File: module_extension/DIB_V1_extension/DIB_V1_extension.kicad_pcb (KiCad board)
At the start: 2 copper layers, 76.1 x 51.5 mm, 12 parts, among them J1 20-pin power socket, J2 28-pin module socket, J3 PROBE, J4 CABLE, J5 PROBE, J6 CABLE

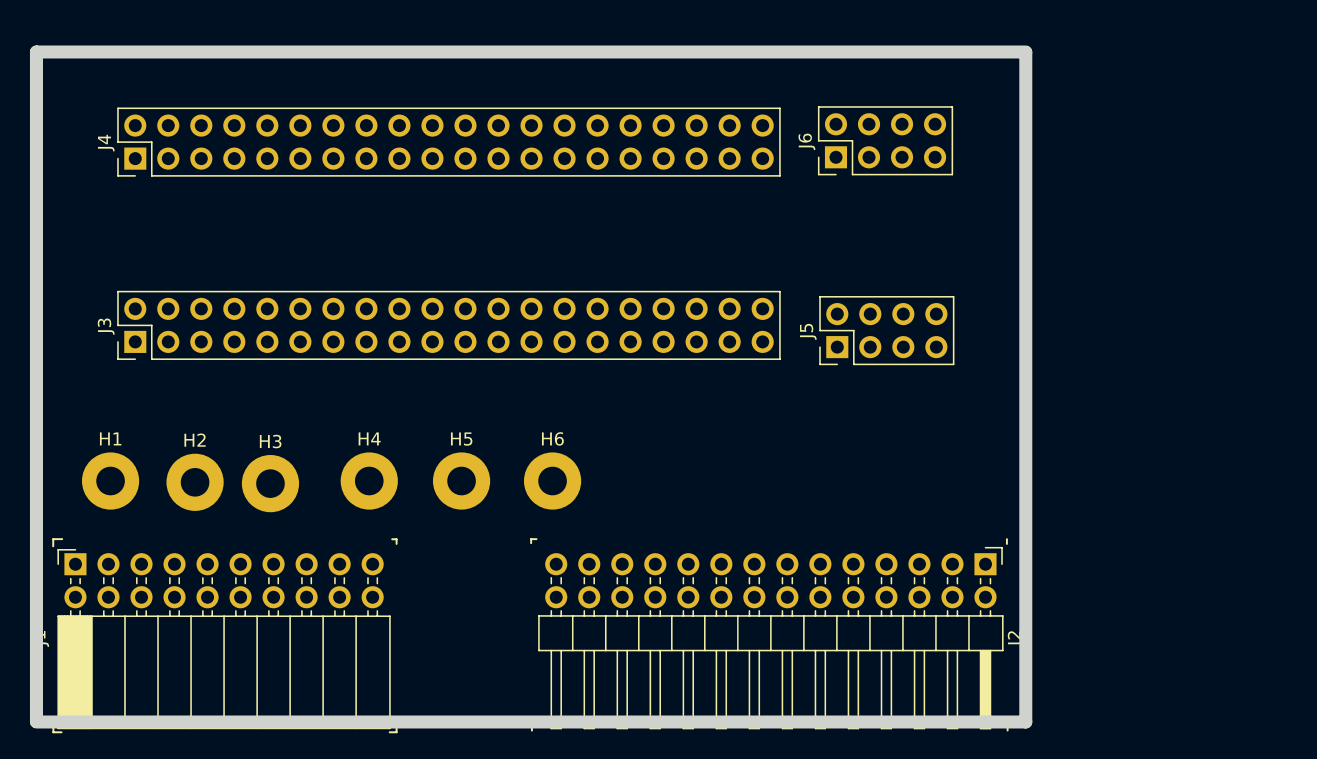
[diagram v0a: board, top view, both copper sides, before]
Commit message: Finished routing, adding pictures and README
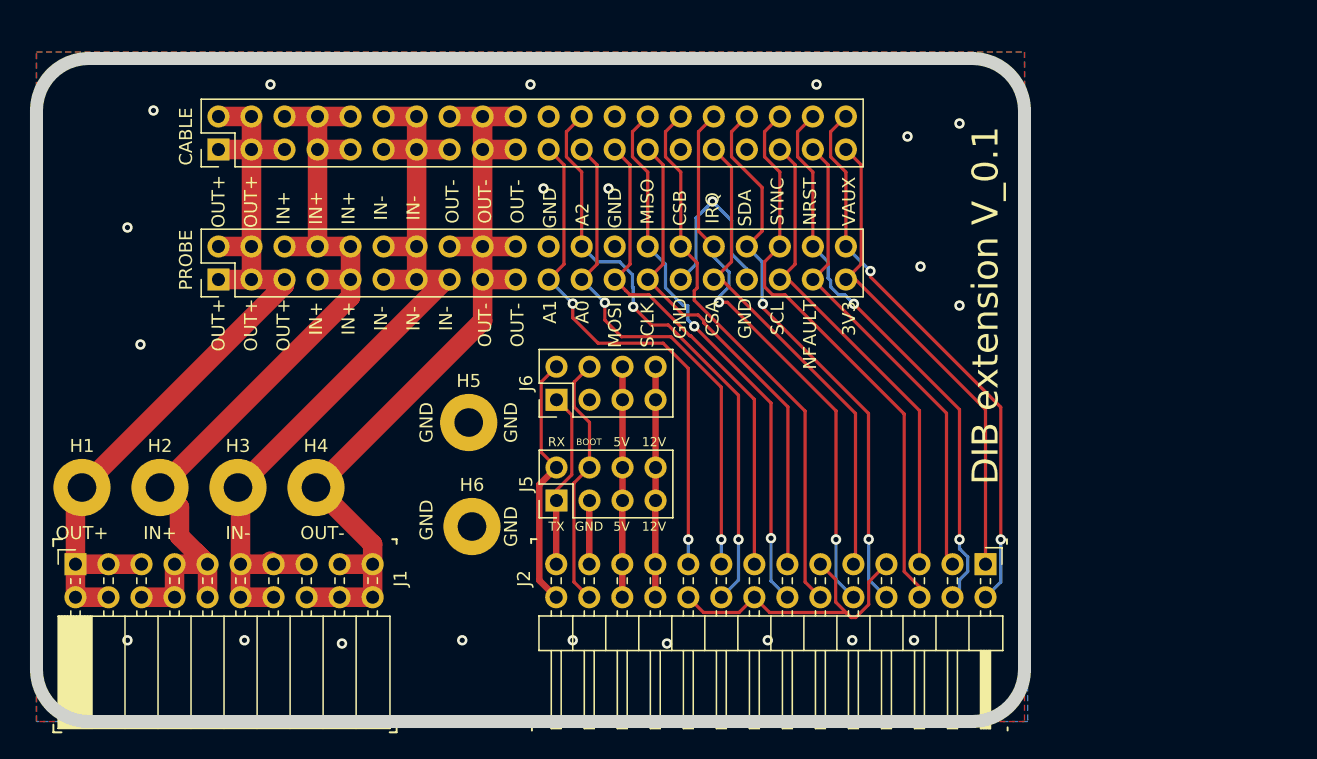
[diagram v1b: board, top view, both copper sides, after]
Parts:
- moved J6 28.5 mm to (113.3, 110.8)
- moved J5 24.6 mm to (113.3, 118.6)
- moved J3 8.00 mm to (87.3, 101.6)
- moved H6 7.12 mm to (106.8, 120.6)
- moved J4 6.44 mm to (87.3, 91.6)
- moved H5 4.53 mm to (106.5, 112.6)
- moved H4 4.13 mm to (94.8, 117.6)
- moved H2 2.73 mm to (82.8, 117.6)
- moved H3 2.52 mm to (88.8, 117.6)
- moved H1 2.26 mm to (76.8, 117.6)
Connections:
- J2 pad 1: (no net) -> DIB_+3V3
- J2 pad 10: (no net) -> DIB_IRQ
- J2 pad 12: (no net) -> DIB_CSB
- J2 pad 13: (no net) -> DIB_SCLK
- J2 pad 14: (no net) -> DIB_MISO
- J2 pad 15: (no net) -> DIB_MOSI
- J2 pad 17: (no net) -> DIB_A0
- J2 pad 18: (no net) -> DIB_A2
- J2 pad 19: (no net) -> DIB_A1
- J2 pad 2: (no net) -> +VAUX
- J2 pad 26: (no net) -> DIB_BOOT
- J2 pad 27: (no net) -> UART_TX
- J2 pad 28: (no net) -> UART_RX
- J2 pad 3: (no net) -> DIB_NFAULT
- J2 pad 4: (no net) -> DIB_NRESET
- J2 pad 5: (no net) -> DIB_SCL
- J2 pad 6: (no net) -> DIB_SYNC
- J2 pad 8: (no net) -> DIB_SDA
- J2 pad 9: (no net) -> DIB_CSA
- J3 pad 1: (no net) -> OUT+
- J3 pad 10: (no net) -> IN+
- J3 pad 11: (no net) -> IN-
- J3 pad 12: (no net) -> IN-
- J3 pad 13: (no net) -> IN-
- J3 pad 14: (no net) -> IN-
- J3 pad 15: (no net) -> IN-
- J3 pad 16: (no net) -> OUT-
- J3 pad 17: (no net) -> OUT-
- J3 pad 18: (no net) -> OUT-
- J3 pad 19: (no net) -> OUT-
- J3 pad 2: (no net) -> OUT+
- J3 pad 20: (no net) -> OUT-
- J3 pad 21: (no net) -> DIB_A1
- J3 pad 22: (no net) -> GND
- J3 pad 23: (no net) -> DIB_A0
- J3 pad 24: (no net) -> DIB_A2
- J3 pad 25: (no net) -> DIB_MOSI
- J3 pad 26: (no net) -> GND
- J3 pad 27: (no net) -> DIB_SCLK
- J3 pad 28: (no net) -> DIB_MISO
- J3 pad 29: (no net) -> GND
- J3 pad 3: (no net) -> OUT+
- J3 pad 30: (no net) -> DIB_CSB
- J3 pad 31: (no net) -> DIB_CSA
- J3 pad 32: (no net) -> DIB_IRQ
- J3 pad 33: (no net) -> GND
- J3 pad 34: (no net) -> DIB_SDA
- J3 pad 35: (no net) -> DIB_SCL
- J3 pad 36: (no net) -> DIB_SYNC
- J3 pad 37: (no net) -> DIB_NFAULT
- J3 pad 38: (no net) -> DIB_NRESET
- J3 pad 39: (no net) -> DIB_+3V3
- J3 pad 4: (no net) -> OUT+
- J3 pad 40: (no net) -> +VAUX
- J3 pad 5: (no net) -> OUT+
- J3 pad 6: (no net) -> IN+
- J3 pad 7: (no net) -> IN+
- J3 pad 8: (no net) -> IN+
- J3 pad 9: (no net) -> IN+
- J4 pad 1: (no net) -> OUT+
- J4 pad 10: (no net) -> IN+
- J4 pad 11: (no net) -> IN-
- J4 pad 12: (no net) -> IN-
- J4 pad 13: (no net) -> IN-
- J4 pad 14: (no net) -> IN-
- J4 pad 15: (no net) -> IN-
- J4 pad 16: (no net) -> OUT-
- J4 pad 17: (no net) -> OUT-
- J4 pad 18: (no net) -> OUT-
- J4 pad 19: (no net) -> OUT-
- J4 pad 2: (no net) -> OUT+
- J4 pad 20: (no net) -> OUT-
- J4 pad 21: (no net) -> DIB_A1
- J4 pad 22: (no net) -> GND
- J4 pad 23: (no net) -> DIB_A0
- J4 pad 24: (no net) -> DIB_A2
- J4 pad 25: (no net) -> DIB_MOSI
- J4 pad 26: (no net) -> GND
- J4 pad 27: (no net) -> DIB_SCLK
- J4 pad 28: (no net) -> DIB_MISO
- J4 pad 29: (no net) -> GND
- J4 pad 3: (no net) -> OUT+
- J4 pad 30: (no net) -> DIB_CSB
- J4 pad 31: (no net) -> DIB_CSA
- J4 pad 32: (no net) -> DIB_IRQ
- J4 pad 33: (no net) -> GND
- J4 pad 34: (no net) -> DIB_SDA
- J4 pad 35: (no net) -> DIB_SCL
- J4 pad 36: (no net) -> DIB_SYNC
- J4 pad 37: (no net) -> DIB_NFAULT
- J4 pad 38: (no net) -> DIB_NRESET
- J4 pad 39: (no net) -> DIB_+3V3
- J4 pad 4: (no net) -> OUT+
- J4 pad 40: (no net) -> +VAUX
- J4 pad 5: (no net) -> OUT+
- J4 pad 6: (no net) -> IN+
- J4 pad 7: (no net) -> IN+
- J4 pad 8: (no net) -> IN+
- J4 pad 9: (no net) -> IN+
- J5 pad 1: (no net) -> UART_TX
- J5 pad 2: (no net) -> UART_RX
- J5 pad 3: (no net) -> GND
- J5 pad 4: (no net) -> DIB_BOOT
- J5 pad 5: (no net) -> 5V
- J5 pad 6: (no net) -> 5V
- J5 pad 7: (no net) -> +12V
- J5 pad 8: (no net) -> +12V
- J6 pad 1: (no net) -> UART_TX
- J6 pad 2: (no net) -> UART_RX
- J6 pad 3: (no net) -> GND
- J6 pad 4: (no net) -> DIB_BOOT
- J6 pad 5: (no net) -> 5V
- J6 pad 6: (no net) -> 5V
- J6 pad 7: (no net) -> +12V
- J6 pad 8: (no net) -> +12V
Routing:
- net IN+: track 0.00 -> 68.8 mm
- net IN-: track 0.00 -> 67.2 mm
- net OUT-: track 0.00 -> 67.0 mm
- net OUT+: track 0.00 -> 66.5 mm
- net DIB_A2: track 0.00 -> 45.3 mm, vias 0 -> 2
- net DIB_SYNC: track 0.00 -> 43.9 mm
- net DIB_NRESET: track 0.00 -> 43.7 mm, vias 0 -> 2
- net DIB_IRQ: track 0.00 -> 43.4 mm, vias 0 -> 2
- net DIB_SDA: track 0.00 -> 43.4 mm, vias 0 -> 2
- net +VAUX: track 0.00 -> 43.4 mm, vias 0 -> 2
- net GND: track 0.00 -> 43.2 mm, vias 0 -> 22
- net DIB_MISO: track 0.00 -> 42.6 mm, vias 0 -> 2
- net DIB_CSB: track 0.00 -> 42.6 mm
- net DIB_A1: track 0.00 -> 40.3 mm, vias 0 -> 2
- net DIB_A0: track 0.00 -> 39.5 mm, vias 0 -> 2
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- added copper zone on B.Cu, net GND
- added copper zone on F.Cu, net GND
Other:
- board size 76.1 x 51.5 mm -> 76 x 51 mm
- board text added: "12V"
- board text added: "3V3"
- board text added: "5V"
- board text added: "A0"
- board text added: "A1"
- board text added: "A2"
- board text added: "BOOT"
- board text added: "CABLE"
- board text added: "CSA"
- board text added: "CSB"
- board text added: "DIB extension V_0.1"
- board text added: "GND"
- board text added: "IN+"
- board text added: "IN-"
- board text added: "IRQ"
- board text added: "MISO"
- board text added: "MOSI"
- board text added: "NFAULT"
- board text added: "NRST"
- board text added: "OUT+"
- board text added: "OUT-"
- board text added: "PROBE"
- board text added: "RX"
- board text added: "SCL"
- board text added: "SCLK"
- board text added: "SDA"
- board text added: "SYNC"
- board text added: "TX"
- board text added: "VAUX"

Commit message: More cooper on power lines
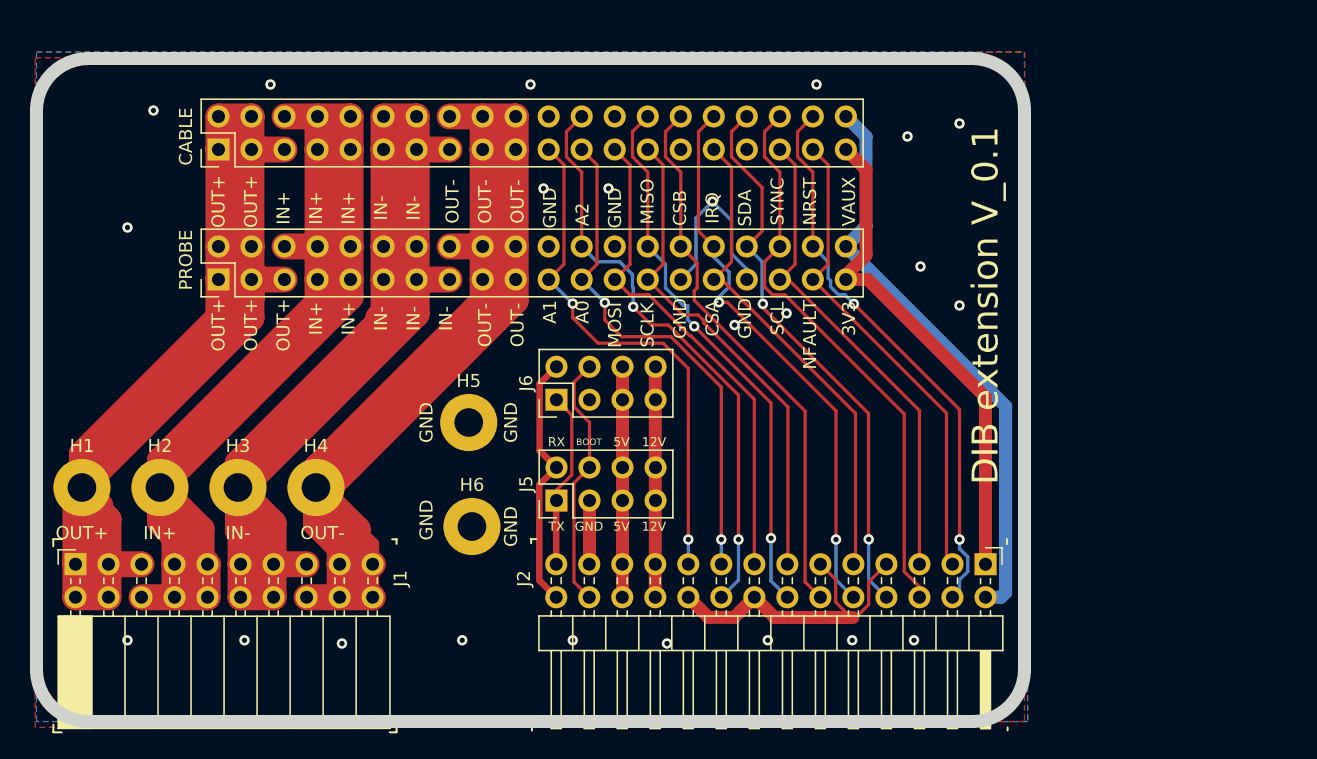
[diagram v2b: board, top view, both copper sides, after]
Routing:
- net OUT+: track 66.5 -> 145.6 mm
- net OUT-: track 67.0 -> 145.6 mm
- net IN+: track 68.8 -> 144.1 mm
- net IN-: track 67.2 -> 134.6 mm
- net +12V: track 17.7 -> 35.5 mm
- net 5V: track 17.7 -> 35.5 mm
- net GND: track 43.2 -> 51.7 mm, vias 22 -> 23
- net +VAUX: track 43.4 -> 44.7 mm, vias 2 -> 0
- net DIB_+3V3: track 37.8 -> 38.6 mm

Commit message: Changing pinout
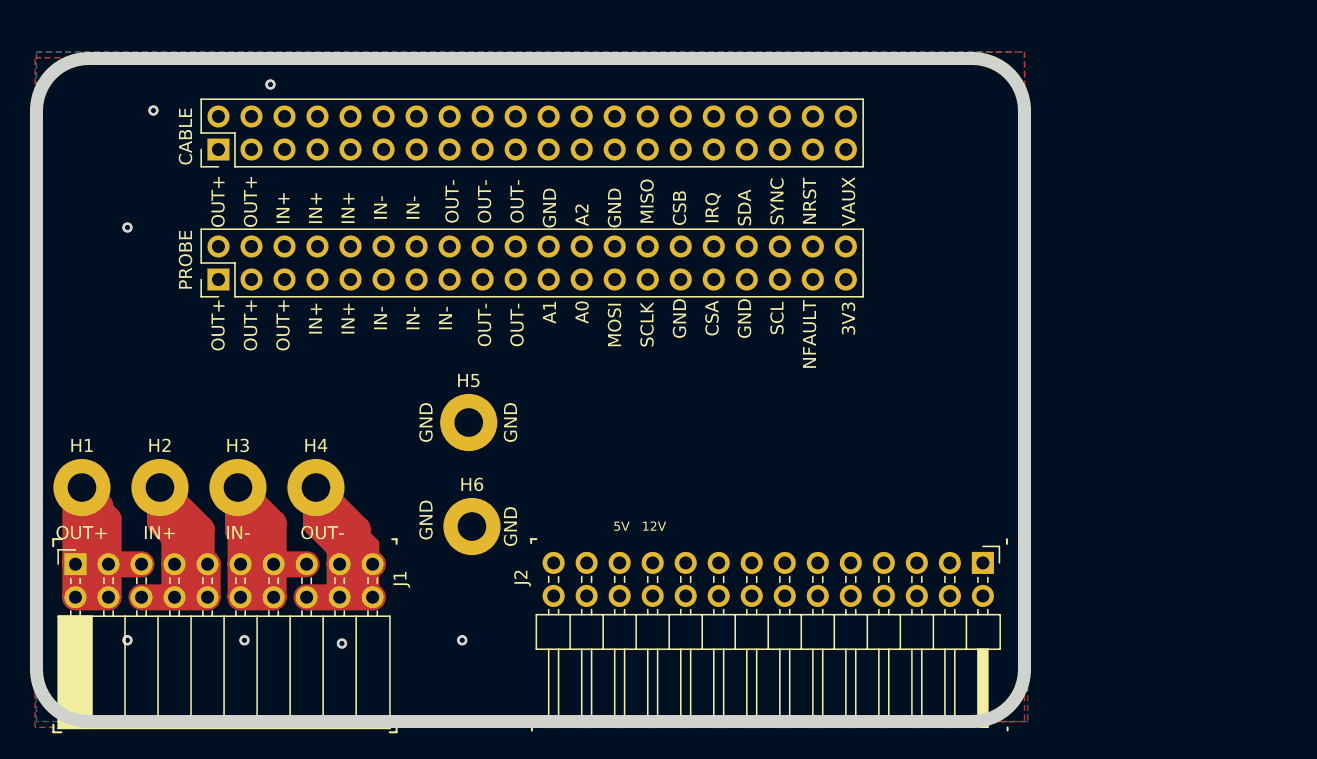
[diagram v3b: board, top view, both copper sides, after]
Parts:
- removed J5: PROBE, Connector_PinHeader_2.54mm:PinHeader_2x04_P2.54mm_Vertical
- removed J6: CABLE, Connector_PinHeader_2.54mm:PinHeader_2x04_P2.54mm_Vertical
- moved J2 0.22 mm to (146.1, 123.4)
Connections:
- J2 pad 1: DIB_+3V3 -> UART_RX
- J2 pad 10: DIB_IRQ -> DIB_A1
- J2 pad 11: GND -> DIB_A2
- J2 pad 12: DIB_CSB -> DIB_A0
- J2 pad 13: DIB_SCLK -> GND
- J2 pad 14: DIB_MISO -> DIB_MOSI
- J2 pad 15: DIB_MOSI -> DIB_MISO
- J2 pad 16: GND -> DIB_SCLK
- J2 pad 17: DIB_A0 -> DIB_CSB
- J2 pad 18: DIB_A2 -> GND
- J2 pad 19: DIB_A1 -> DIB_IRQ
- J2 pad 2: +VAUX -> UART_TX
- J2 pad 20: GND -> DIB_CSA
- J2 pad 21: +12V -> DIB_SDA
- J2 pad 22: +12V -> GND
- J2 pad 23: 5V -> DIB_SYNC
- J2 pad 24: 5V -> DIB_SCL
- J2 pad 25: GND -> DIB_NRESET
- J2 pad 26: DIB_BOOT -> DIB_NFAULT
- J2 pad 27: UART_TX -> +VAUX
- J2 pad 28: UART_RX -> DIB_+3V3
- J2 pad 3: DIB_NFAULT -> DIB_BOOT
- J2 pad 4: DIB_NRESET -> GND
- J2 pad 5: DIB_SCL -> 5V
- J2 pad 6: DIB_SYNC -> 5V
- J2 pad 7: GND -> +12V
- J2 pad 8: DIB_SDA -> +12V
- J2 pad 9: DIB_CSA -> GND
- J3 pad 10: IN+ -> IN-
- J3 pad 13: IN- -> OUT-
- J3 pad 14: IN- -> OUT-
- J3 pad 15: IN- -> OUT-
- J3 pad 17: OUT- -> DIB_+3V3
- J3 pad 18: OUT- -> +VAUX
- J3 pad 19: OUT- -> DIB_NFAULT
- J3 pad 20: OUT- -> DIB_NRESET
- J3 pad 21: DIB_A1 -> DIB_SCL
- J3 pad 22: GND -> DIB_SYNC
- J3 pad 23: DIB_A0 -> GND
- J3 pad 24: DIB_A2 -> DIB_SDA
- J3 pad 25: DIB_MOSI -> DIB_CSA
- J3 pad 26: GND -> DIB_IRQ
- J3 pad 27: DIB_SCLK -> GND
- J3 pad 28: DIB_MISO -> DIB_CSB
- J3 pad 29: GND -> DIB_SCLK
- J3 pad 30: DIB_CSB -> DIB_MISO
- J3 pad 31: DIB_CSA -> DIB_MOSI
- J3 pad 32: DIB_IRQ -> GND
- J3 pad 33: GND -> DIB_A0
- J3 pad 34: DIB_SDA -> DIB_A2
- J3 pad 35: DIB_SCL -> DIB_A1
- J3 pad 36: DIB_SYNC -> DIB_BOOT
- J3 pad 37: DIB_NFAULT -> UART_TX
- J3 pad 38: DIB_NRESET -> UART_RX
- J3 pad 39: DIB_+3V3 -> 5V
- J3 pad 40: +VAUX -> +12V
- J3 pad 5: OUT+ -> IN+
- J3 pad 9: IN+ -> IN-
- J4 pad 10: IN+ -> IN-
- J4 pad 13: IN- -> OUT-
- J4 pad 14: IN- -> OUT-
- J4 pad 15: IN- -> OUT-
- J4 pad 17: OUT- -> DIB_+3V3
- J4 pad 18: OUT- -> +VAUX
- J4 pad 19: OUT- -> DIB_NFAULT
- J4 pad 20: OUT- -> DIB_NRESET
- J4 pad 21: DIB_A1 -> DIB_SCL
- J4 pad 22: GND -> DIB_SYNC
- J4 pad 23: DIB_A0 -> GND
- J4 pad 24: DIB_A2 -> DIB_SDA
- J4 pad 25: DIB_MOSI -> DIB_CSA
- J4 pad 26: GND -> DIB_IRQ
- J4 pad 27: DIB_SCLK -> GND
- J4 pad 28: DIB_MISO -> DIB_CSB
- J4 pad 29: GND -> DIB_SCLK
- J4 pad 30: DIB_CSB -> DIB_MISO
- J4 pad 31: DIB_CSA -> DIB_MOSI
- J4 pad 32: DIB_IRQ -> GND
- J4 pad 33: GND -> DIB_A0
- J4 pad 34: DIB_SDA -> DIB_A2
- J4 pad 35: DIB_SCL -> DIB_A1
- J4 pad 36: DIB_SYNC -> DIB_BOOT
- J4 pad 37: DIB_NFAULT -> UART_TX
- J4 pad 38: DIB_NRESET -> UART_RX
- J4 pad 39: DIB_+3V3 -> 5V
- J4 pad 40: +VAUX -> +12V
- J4 pad 5: OUT+ -> IN+
- J4 pad 9: IN+ -> IN-
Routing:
- net OUT+: track 145.6 -> 32.5 mm
- net OUT-: track 145.6 -> 33.8 mm
- net IN+: track 144.1 -> 33.5 mm
- net IN-: track 134.6 -> 33.1 mm
- net GND: track 51.7 -> 0.00 mm, vias 23 -> 7
- net DIB_A2: track 45.3 -> 0.00 mm, vias 2 -> 0
- net +VAUX: track 44.7 -> 0.00 mm
- net DIB_SYNC: track 43.9 -> 0.00 mm
- net DIB_NRESET: track 43.7 -> 0.00 mm, vias 2 -> 0
- net DIB_IRQ: track 43.4 -> 0.00 mm, vias 2 -> 0
- net DIB_SDA: track 43.4 -> 0.00 mm, vias 2 -> 0
- net DIB_MISO: track 42.6 -> 0.00 mm, vias 2 -> 0
- net DIB_CSB: track 42.6 -> 0.00 mm
- net DIB_A1: track 40.3 -> 0.00 mm, vias 2 -> 0
- net DIB_A0: track 39.5 -> 0.00 mm, vias 2 -> 0
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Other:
- board text removed: "BOOT"
- board text removed: "DIB extension V_0.1"
- board text removed: "RX"
- board text removed: "TX"
